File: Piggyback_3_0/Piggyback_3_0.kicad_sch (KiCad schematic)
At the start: 51 parts, among them J1 Conn_01x06_Female, J2 Conn_01x23_Female, J3 USB_C_Receptacle_USB2.0, J5 Conn_01x06_Female, SW1 MX_SW_solder, SW10 MX_SW_solder, SW11 MX_SW_solder, SW12 MX_SW_solder, SW13 MX_SW_solder, SW14 MX_SW_solder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

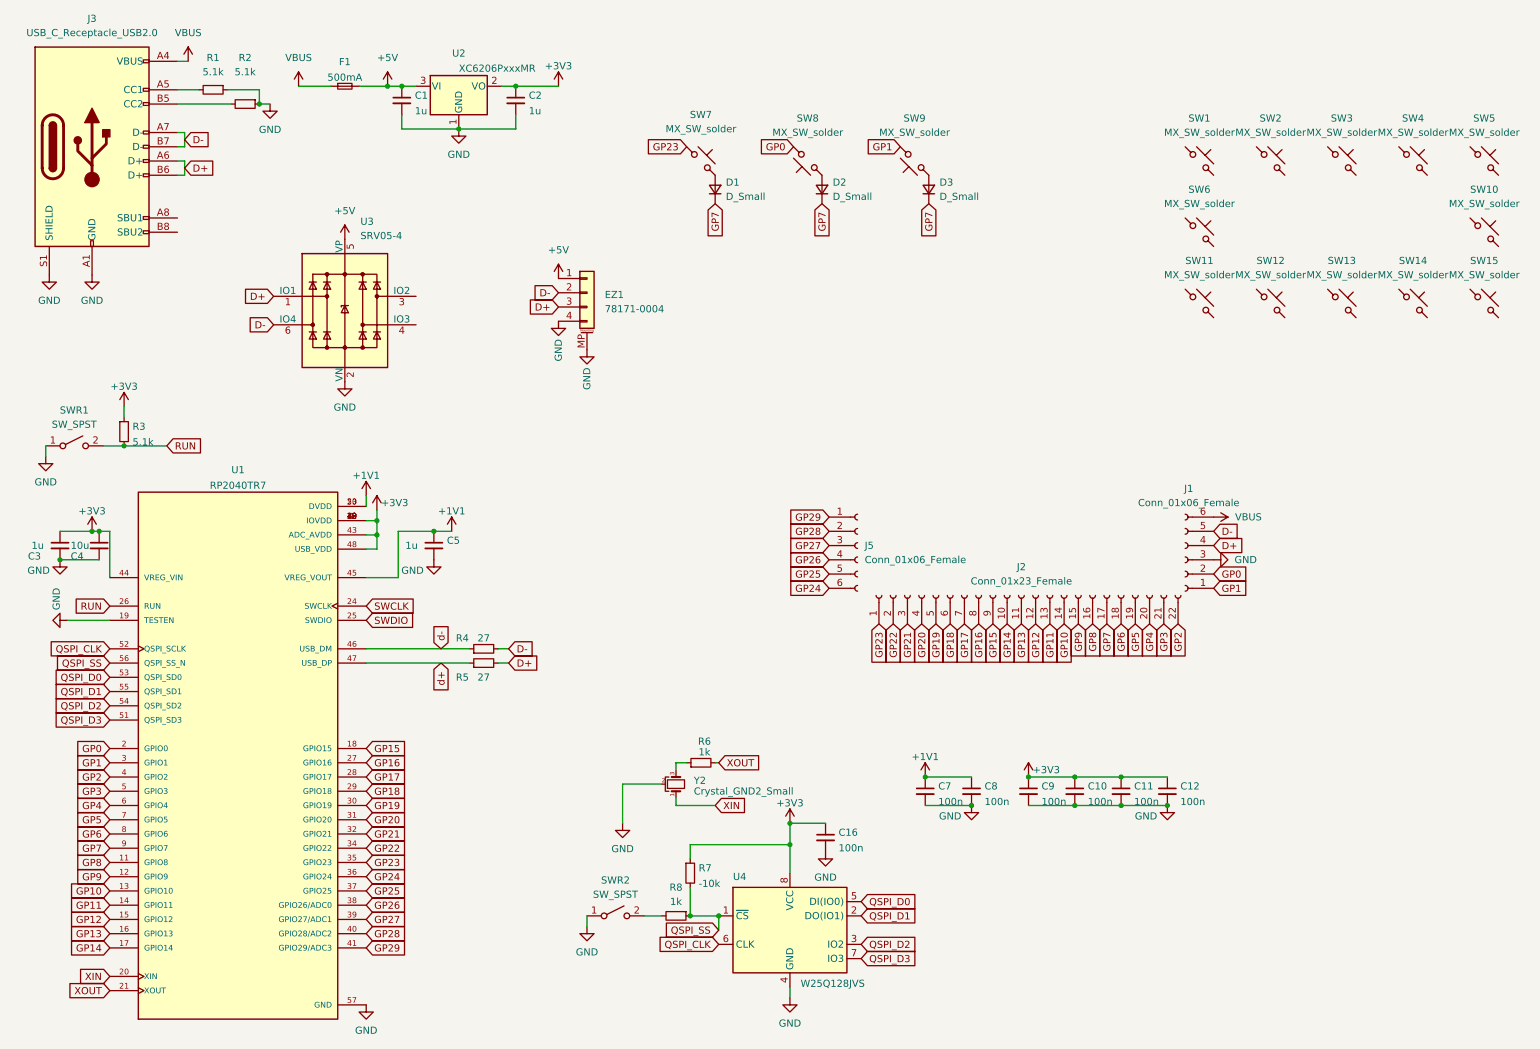
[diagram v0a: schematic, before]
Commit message: add piggyback 3
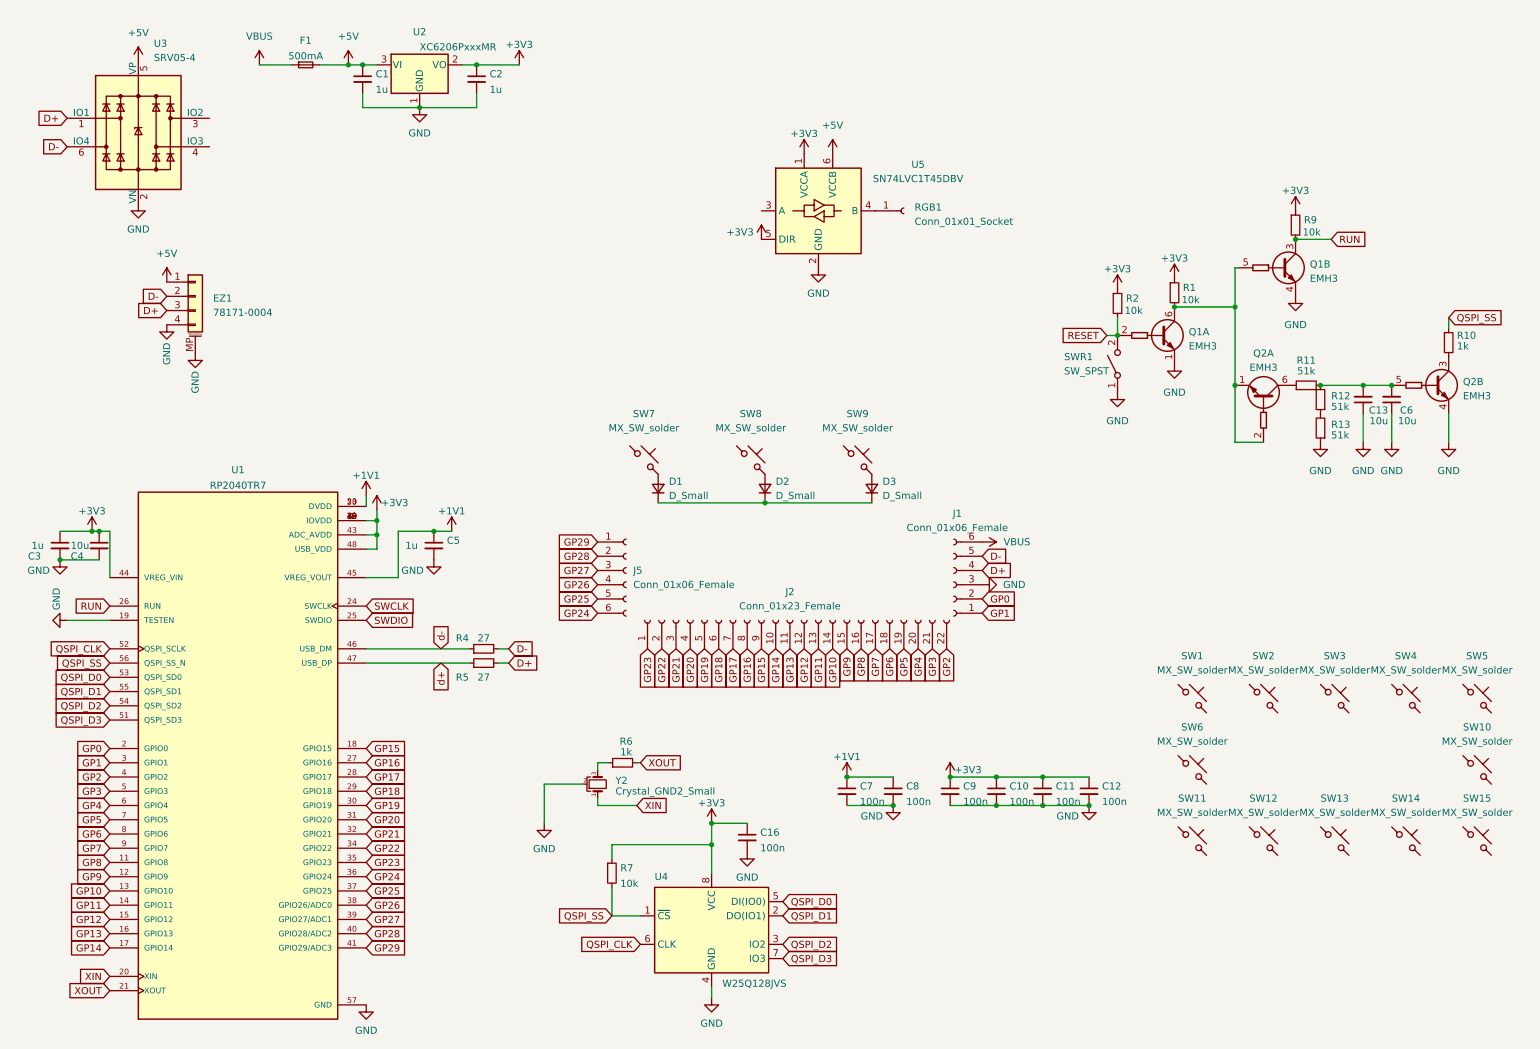
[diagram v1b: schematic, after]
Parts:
- removed J3: USB_C_Receptacle_USB2.0, Connector_USB:USB_C_Receptacle_HRO_TYPE-C-31-M-12, symbol Connector:USB_C_Receptacle_USB2.0
- removed R3: 5.1k, Resistor_SMD:R_0402_1005Metric, symbol Device:R_Small
- removed R8: 1k, Resistor_SMD:R_0402_1005Metric, symbol Device:R_Small
- removed SWR2: SW_SPST, Button_Switch_SMD:SW_Push_SPST_NO_Alps_SKRK, symbol Switch:SW_SPST
- added C13, C6: 10u, Capacitor_SMD:C_0402_1005Metric, symbol Device:C_Small
- added Q1, Q2: EMH3, Package_TO_SOT_SMD:SOT-563, symbol Transistor_BJT:EMH3
- added R10: 1k, Resistor_SMD:R_0402_1005Metric, symbol Device:R_Small
- added R11, R12, R13: 51k, Resistor_SMD:R_0402_1005Metric, symbol Device:R_Small
- added R9: 10k, Resistor_SMD:R_0402_1005Metric, symbol Device:R_Small
- added RGB1: Conn_01x01_Socket, Connector_PinSocket_2.54mm:PinSocket_1x01_P2.54mm_Vertical, symbol Connector:Conn_01x01_Socket
- added U5: SN74LVC1T45DBV, Package_TO_SOT_SMD:SOT-23-6, symbol Logic_LevelTranslator:SN74LVC1T45DBV
- R1, R2: value 5.1k -> 10k
- R7: value -10k -> 10k
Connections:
- net +3V3: now also R1.1, R2.1, R9.1, U5.1 (VCCA), U5.5 (DIR)
- net +5V: now also U5.6 (VCCB)
- net GND: now also C13.1, C6.1, Q1.1 (E1), Q1.4 (E2), Q2.4 (E2), R13.1, U5.2 (GND); no longer R1.1, R2.1
- net GP0: no longer SW8.2
- net GP1: no longer SW9.2
- net GP23: no longer SW7.1
- net GP7: no longer D1.1 (K), D2.1 (K), D3.1 (K)
- net QSPI_SS: now also R10.1
- net RUN: now also Q1.3 (C2), R9.2; no longer SWR1.2 (B)
- net at R1.2: now also Q1.5 (B2), Q1.6 (C1), Q2.1 (E1), Q2.2 (B1)
- net RESET: now reaches R2.2
- net RESET: now also SWR1.2 (B), Q1.2 (B1)
- net at D2.2 (A): now also SW8.2; no longer SW8.1
- net at SW9.1: no longer D3.2 (A)
- new net: D1.1 (K), D2.1 (K), D3.1 (K)
- new net: D3.2 (A), SW9.2
- new net: Q2.6 (C1), R11.1
- new net: C13.2, C6.2, Q2.5 (B2), R11.2, R12.2
- new net: RGB1.1 (Pin_1), U5.4 (B)
- new net: R12.1, R13.2
- new net: Q2.3 (C2), R10.2
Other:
- moved on the sheet: C1, C10, C11, C12, C16, C2, C7, C8, C9, D1, D2, D3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
